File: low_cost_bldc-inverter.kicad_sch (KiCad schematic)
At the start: 23 parts, among them Q1 DMN61D8LQ, Q2 DMN61D8LQ, Q3 BC808W, Q4 BC818W, Q5 DMG3406L, Q6 DMG3406L, Q7 BC808W, Q8 BC818W

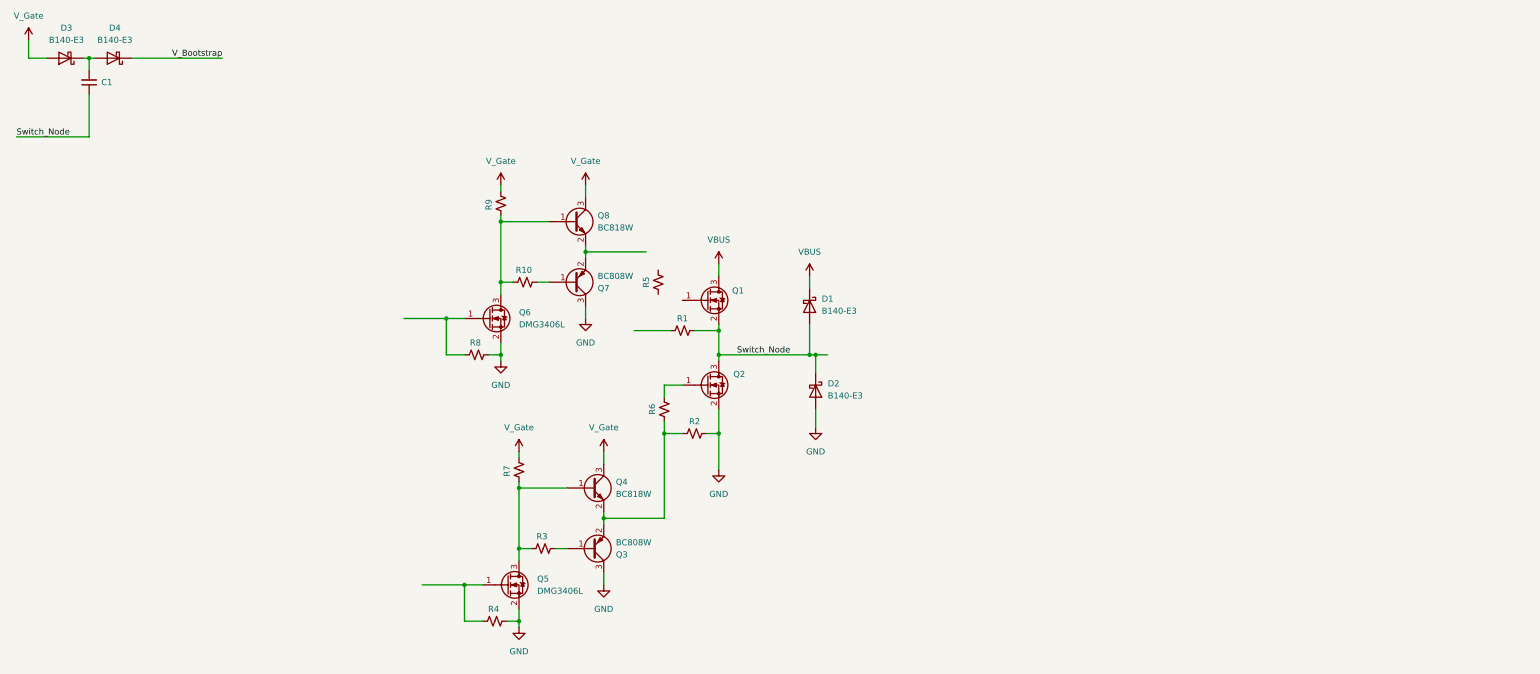
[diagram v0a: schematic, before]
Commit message: Top-only inverter layout
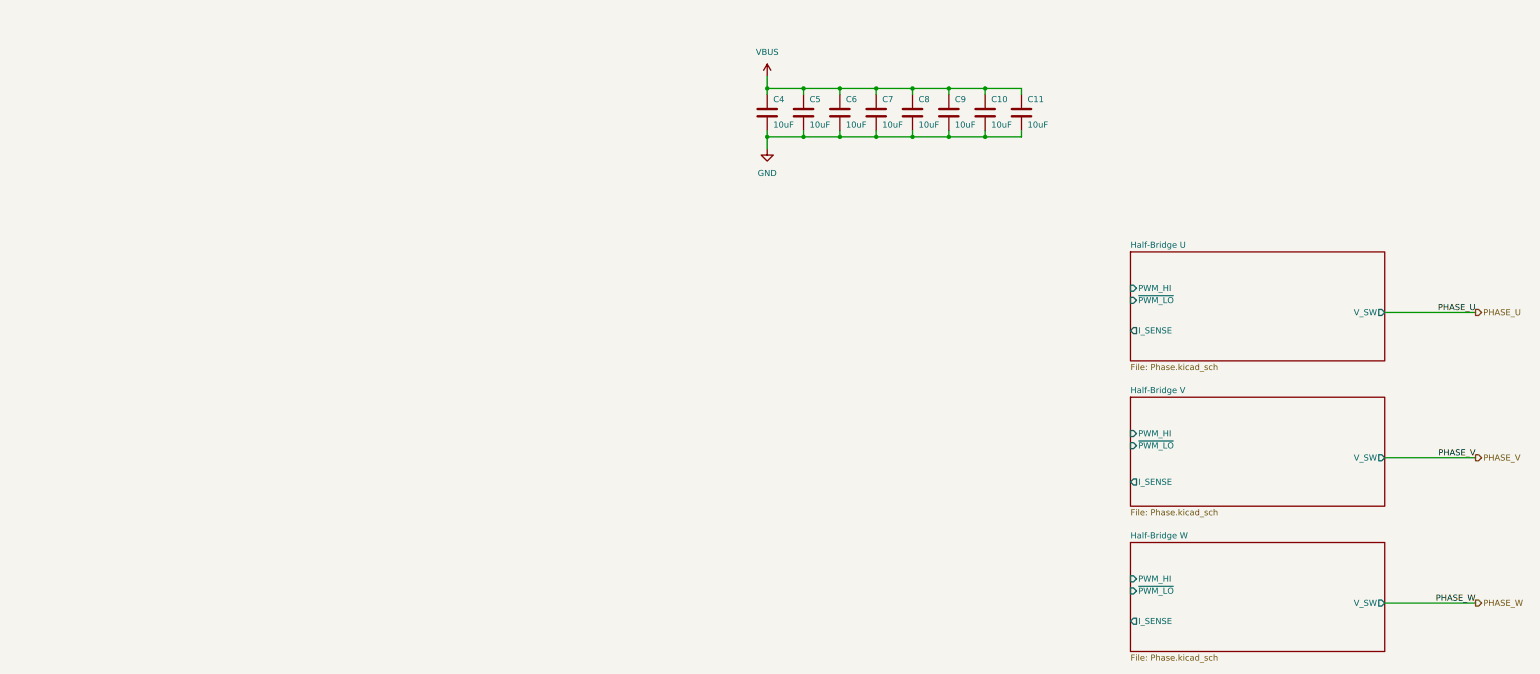
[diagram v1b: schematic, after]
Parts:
- removed C1: C_Small, symbol Device:C_Small
- removed D1, D2, D3, D4: B140-E3, Diode_SMD:D_SMA, symbol Diode:B140-E3
- removed Q1, Q2: DMN61D8LQ, Package_TO_SOT_SMD:SOT-23, symbol Transistor_FET:DMN61D8LQ
- removed Q3, Q7: BC808W, Package_TO_SOT_SMD:SOT-323_SC-70, symbol Transistor_BJT:BC808W
- removed Q4, Q8: BC818W, Package_TO_SOT_SMD:SOT-323_SC-70, symbol Transistor_BJT:BC818W
- removed Q5, Q6: DMG3406L, Package_TO_SOT_SMD:SOT-23, symbol Transistor_FET:DMG3406L
- removed R1, R10, R2, R3, R4, R5, R6, R7, R8, R9: 10k, symbol Device:R_Small_US
- added C10, C11, C4, C5, C6, C7, C8, C9: 10uF, Capacitor_SMD:C_1206_3216Metric, symbol Device:C
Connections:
- net GND: now also C10.2, C11.2, C4.2, C5.2, C6.2, C7.2, C8.2, C9.2
- net VBUS: now also C10.1, C11.1, C4.1, C5.1, C6.1, C7.1, C8.1, C9.1
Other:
- added sheet Half-Bridge U (Phase.kicad_sch)
- added sheet Half-Bridge V (Phase.kicad_sch)
- added sheet Half-Bridge W (Phase.kicad_sch)
- title: (none) -> FreeWheel
